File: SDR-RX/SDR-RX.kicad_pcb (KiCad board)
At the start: 2 copper layers, 53 x 51 mm, 49 parts, among them Q1 S8050, Q2 S8050, U1 Si4734-D60-GU, U2 ESP32-WROOM-32, U3 LD1117S33TR_SOT223, Y1 32.768kHz

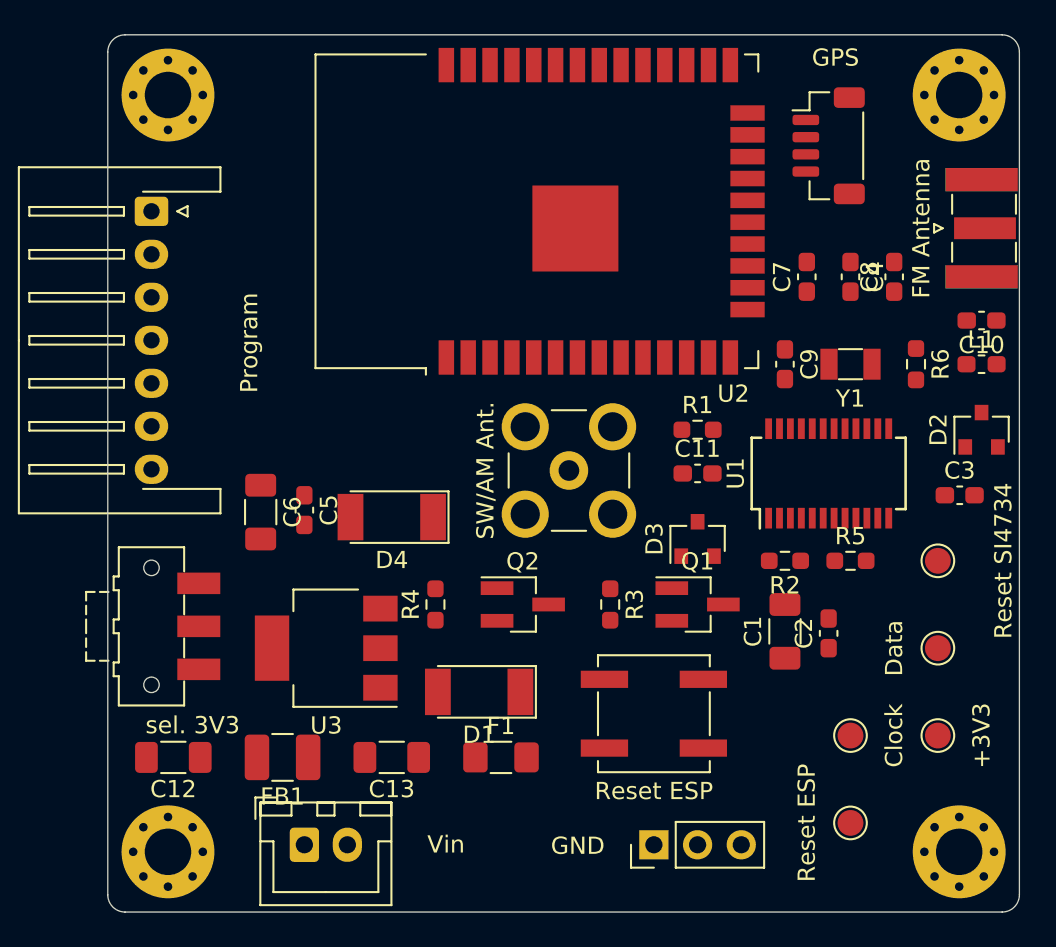
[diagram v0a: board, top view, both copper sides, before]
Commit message: routed without GND
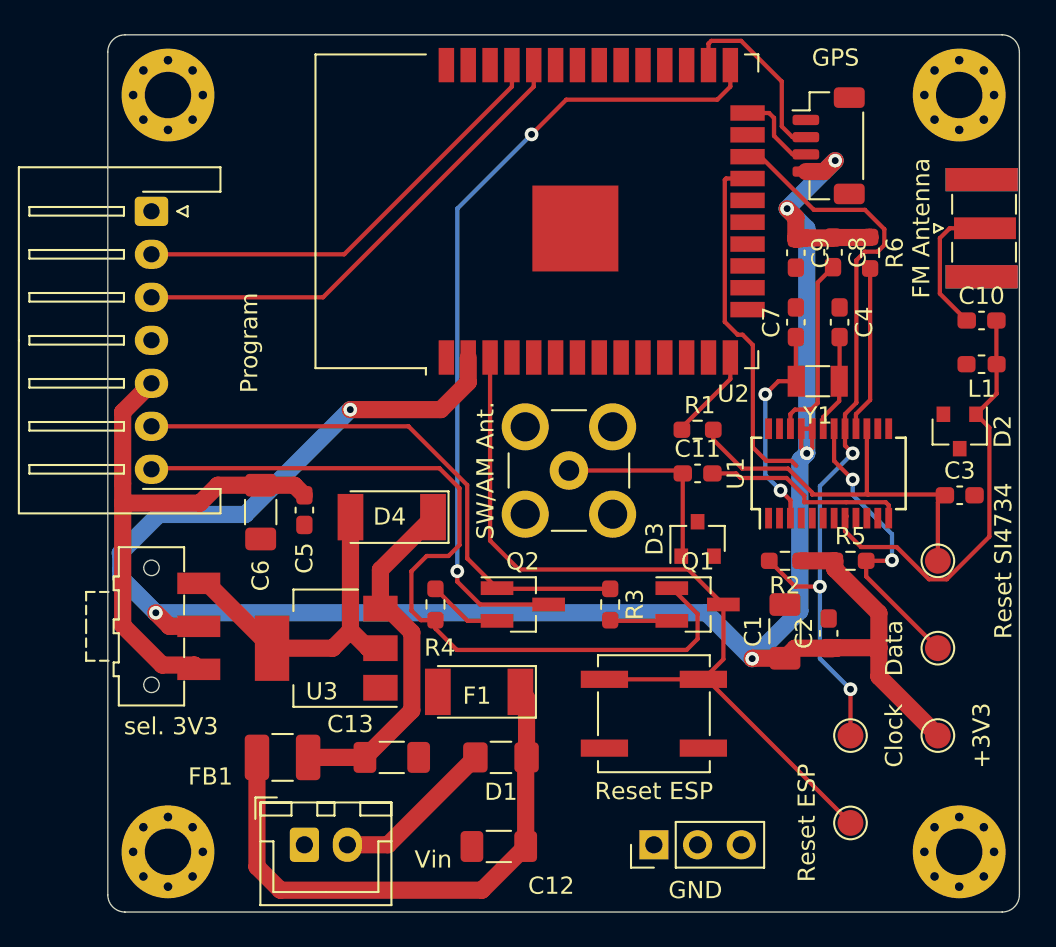
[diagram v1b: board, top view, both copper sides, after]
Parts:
- moved C12 19.6 mm to (398.4, 92.9)
- moved R6 7.00 mm to (420.0, 58.3)
- moved C9 6.51 mm to (415.7, 58.3)
- moved C8 3.83 mm to (417.9, 58.3), turned to 270 degrees
- moved C4 2.72 mm to (418.2, 62.4)
- moved C7 2.72 mm to (415.7, 62.4)
- moved Y1 2.15 mm to (417.0, 65.8)
- moved D2 1.27 mm to (425.2, 68.7), turned to 270 degrees
- turned C10 to 0 degrees
- turned C13 to 0 degrees
- turned L1 to 180 degrees
- turned R1 to 180 degrees
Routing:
- net +3V3: track 0.00 -> 135.1 mm, vias 0 -> 6
- net Net-(J1-Pad7): track 0.00 -> 49.1 mm
- net Net-(Q1-Pad3): track 0.00 -> 48.3 mm
- net Net-(Q2-Pad3): track 0.00 -> 47.6 mm, vias 0 -> 2
- net Net-(R2-Pad2): track 0.00 -> 45.9 mm, vias 0 -> 3
- net Net-(R5-Pad2): track 0.00 -> 38.8 mm, vias 0 -> 2
- net Net-(J1-Pad6): track 0.00 -> 33.1 mm
- net Net-(C12-Pad1): track 0.00 -> 32.8 mm
- net Net-(C5-Pad1): track 0.00 -> 32.0 mm
- net Net-(J1-Pad3): track 0.00 -> 28.5 mm
- net Net-(J1-Pad2): track 0.00 -> 26.2 mm
- net Net-(C10-Pad2): track 0.00 -> 24.9 mm
- net Net-(C3-Pad1): track 0.00 -> 23.3 mm
- net Net-(C13-Pad1): track 0.00 -> 20.7 mm
- net Net-(D4-Pad2): track 0.00 -> 19.6 mm
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
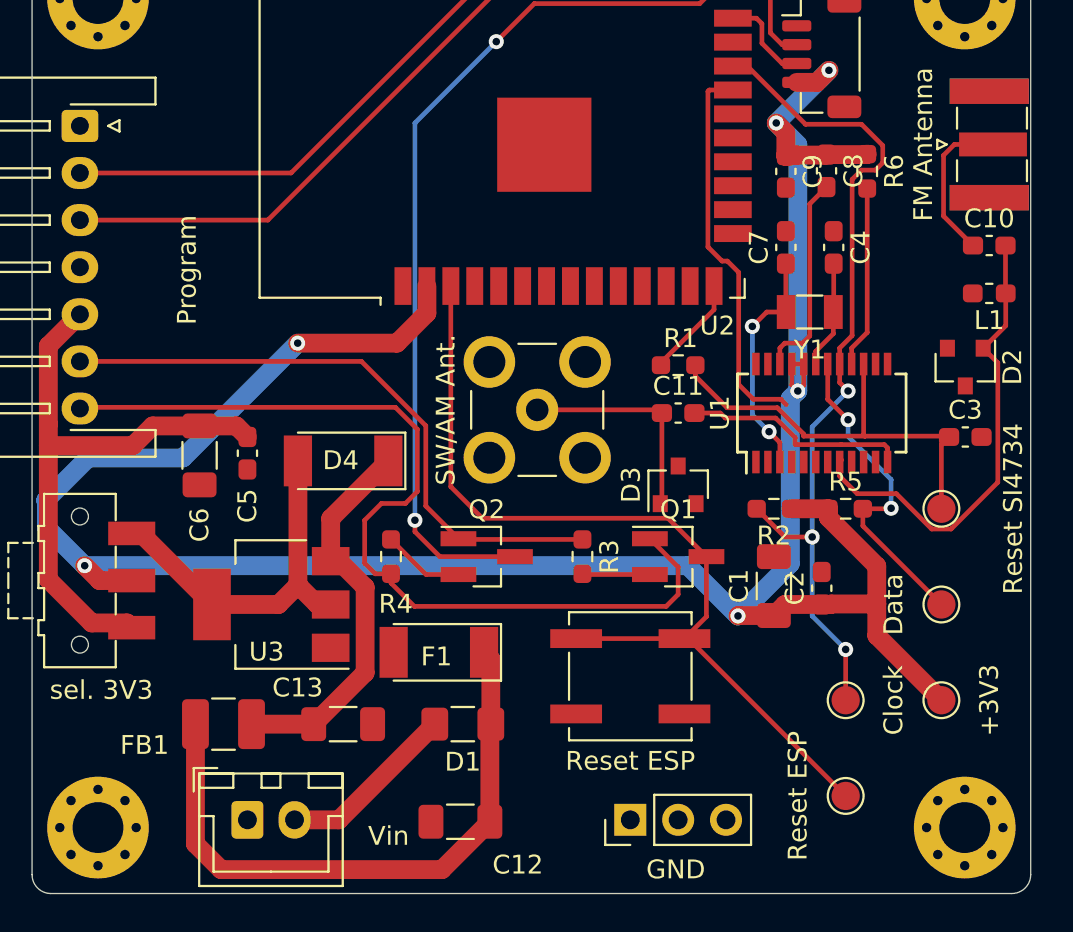
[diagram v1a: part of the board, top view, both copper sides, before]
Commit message: closed misssing copper
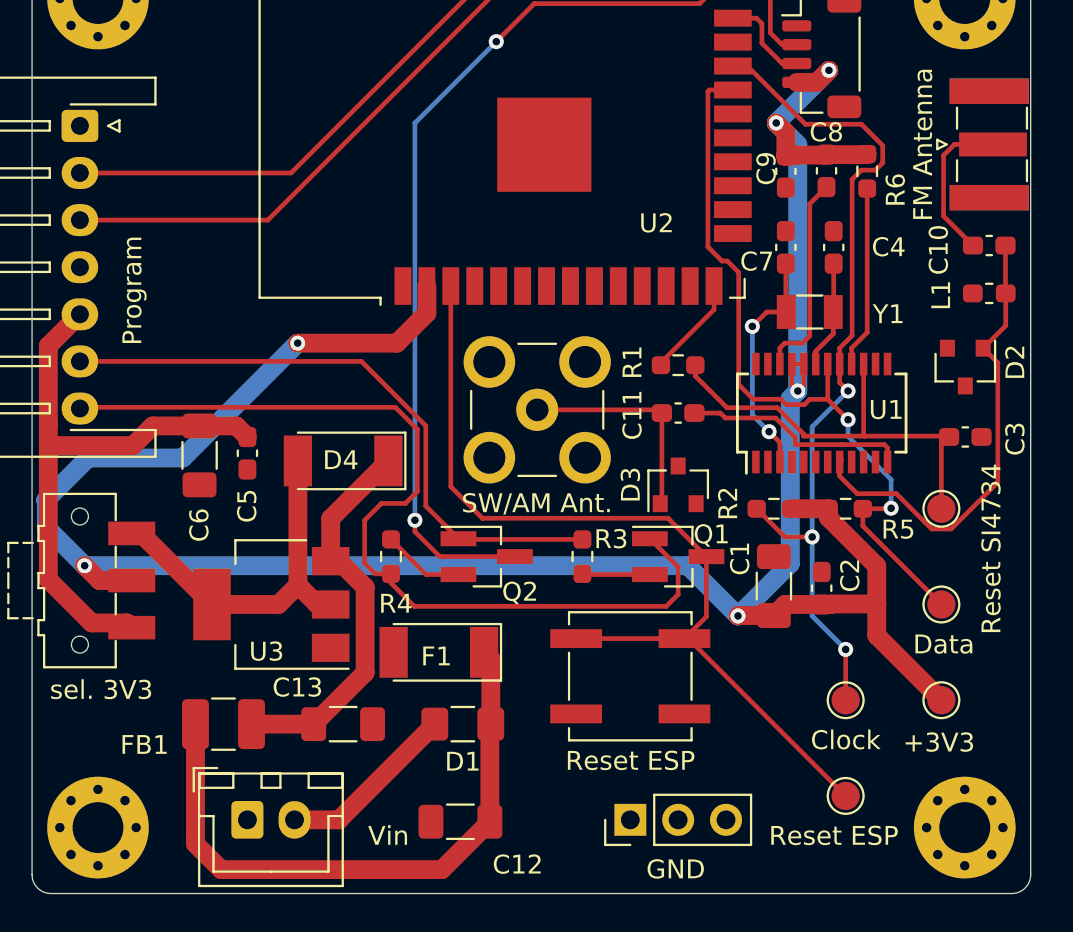
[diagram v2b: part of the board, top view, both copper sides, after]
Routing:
- net Net-(R5-Pad2): track 38.8 -> 41.1 mm

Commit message: PCB routed
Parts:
- added ?: , , F.Cu at (410.0, 95.4)
- moved Vin  1.27 mm to (388.4, 92.8)
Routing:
- net GND: track 0.00 -> 63.8 mm, vias 0 -> 20
- net +3V3: track 135.1 -> 118.8 mm
- net Net-(J1-Pad6): track 33.1 -> 35.0 mm
- net Net-(J1-Pad3): track 28.5 -> 30.1 mm, vias 0 -> 1
- net Net-(J1-Pad2): track 26.2 -> 27.6 mm, vias 0 -> 1
- net Net-(F1-Pad1): track 9.55 -> 8.28 mm
- net Net-(Q2-Pad3): track 47.6 -> 46.9 mm
- added copper zone on B.Cu, net GND
- added copper zone on F.Cu, net GND
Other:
- board text added: "3V3"
- board text added: "DTR"
- board text added: "GND"
- board text added: "NC"
- board text added: "RTS"
- board text added: "RX"
- board text added: "Rst SI4734"
- board text added: "TX"
- board text added: "Vin"

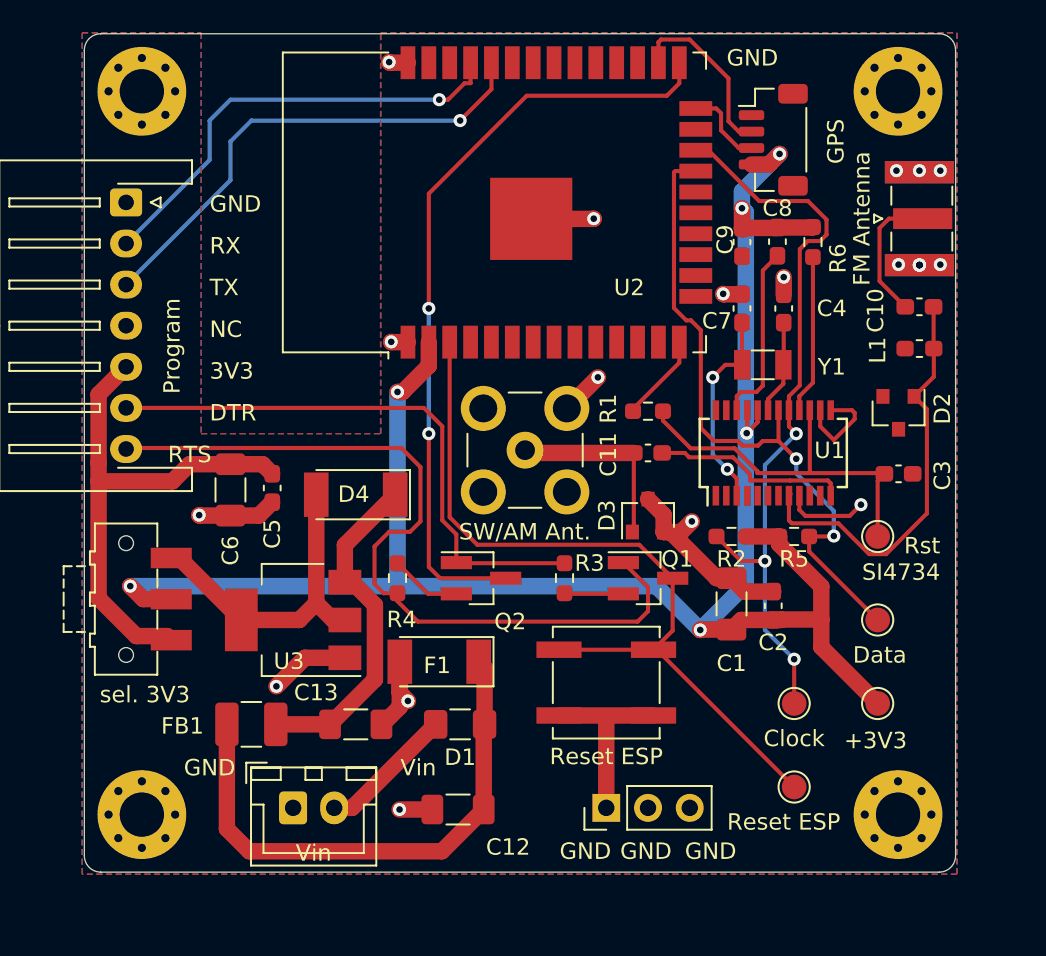
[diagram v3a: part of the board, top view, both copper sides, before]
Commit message: sticked back and front GND zones with vias
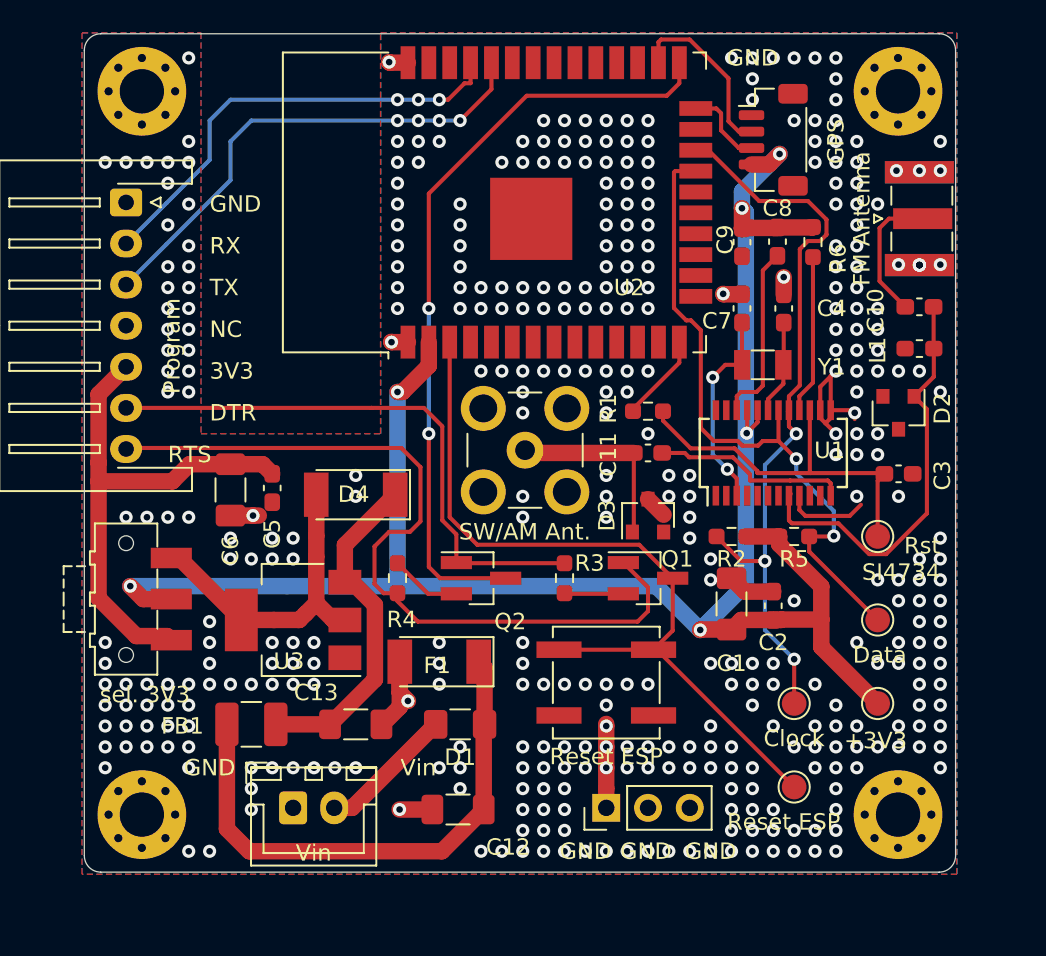
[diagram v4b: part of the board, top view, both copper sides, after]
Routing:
- net GND: track 63.8 -> 39.4 mm, vias 20 -> 395
- net Net-(J1-Pad2): vias 1 -> 3
- net Net-(J1-Pad3): vias 1 -> 4

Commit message: removed obsolete GND vias
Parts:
- moved C2 266.1 mm to (152.2, 99.5)
- moved C3 266.1 mm to (159.8, 91.5)
- moved D2 266.1 mm to (159.8, 87.8)
- moved GPS 266.1 mm to (152.2, 71.2)
- moved U1 266.1 mm to (152.2, 90.2)
- moved ? 266.1 mm to (144.6, 114.5)
- moved C1 266.1 mm to (149.6, 99.4)
- moved C10 266.1 mm to (161.1, 81.3)
- moved C11 266.1 mm to (144.6, 90.2)
- moved C12 266.1 mm to (133.0, 111.9)
- moved C13 266.1 mm to (126.8, 106.7)
- moved C4 266.1 mm to (152.8, 81.4)
- moved C5 266.1 mm to (121.7, 92.4)
- moved C7 266.1 mm to (150.3, 81.4)
- moved C9 266.1 mm to (150.3, 77.4)
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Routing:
- net GND: vias 395 -> 182
- net Net-(J1-Pad3): vias 4 -> 1
- net Net-(J1-Pad2): vias 3 -> 1

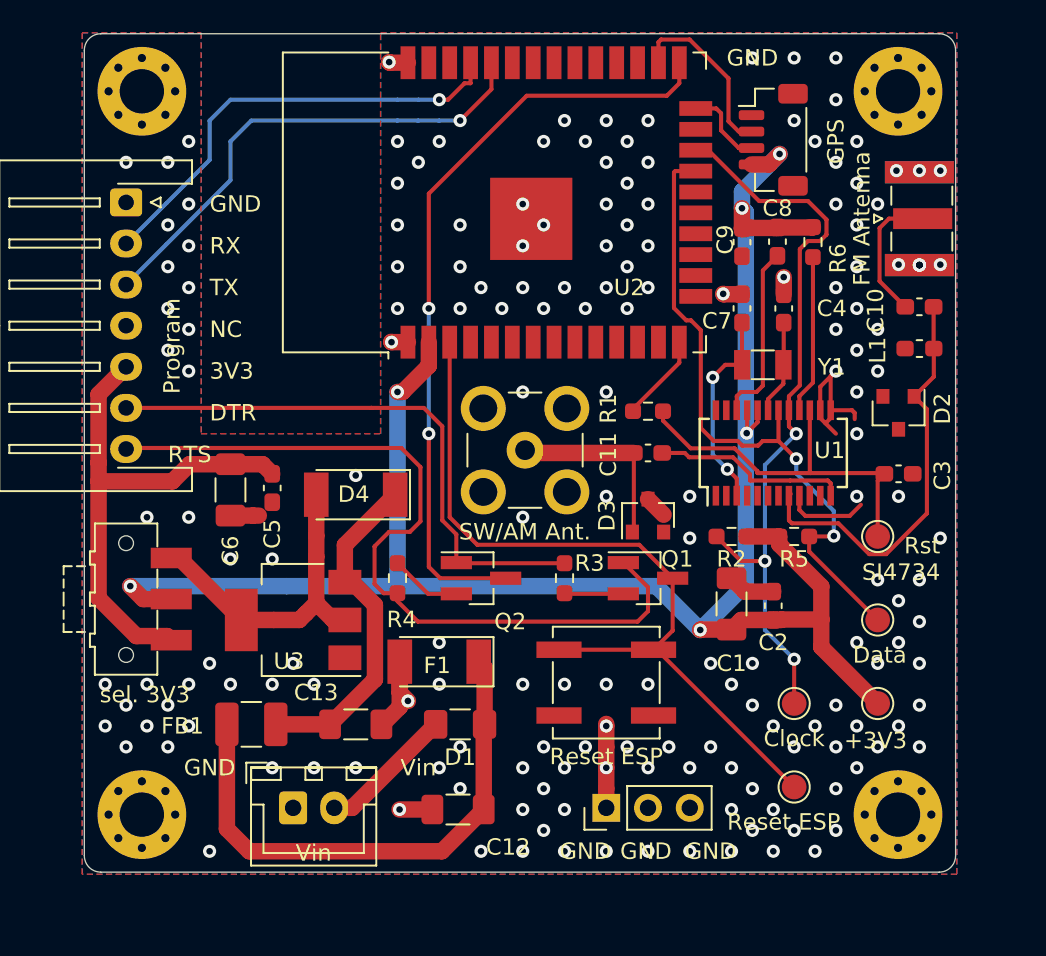
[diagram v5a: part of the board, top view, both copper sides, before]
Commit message: Added BOM and schematics.pdf
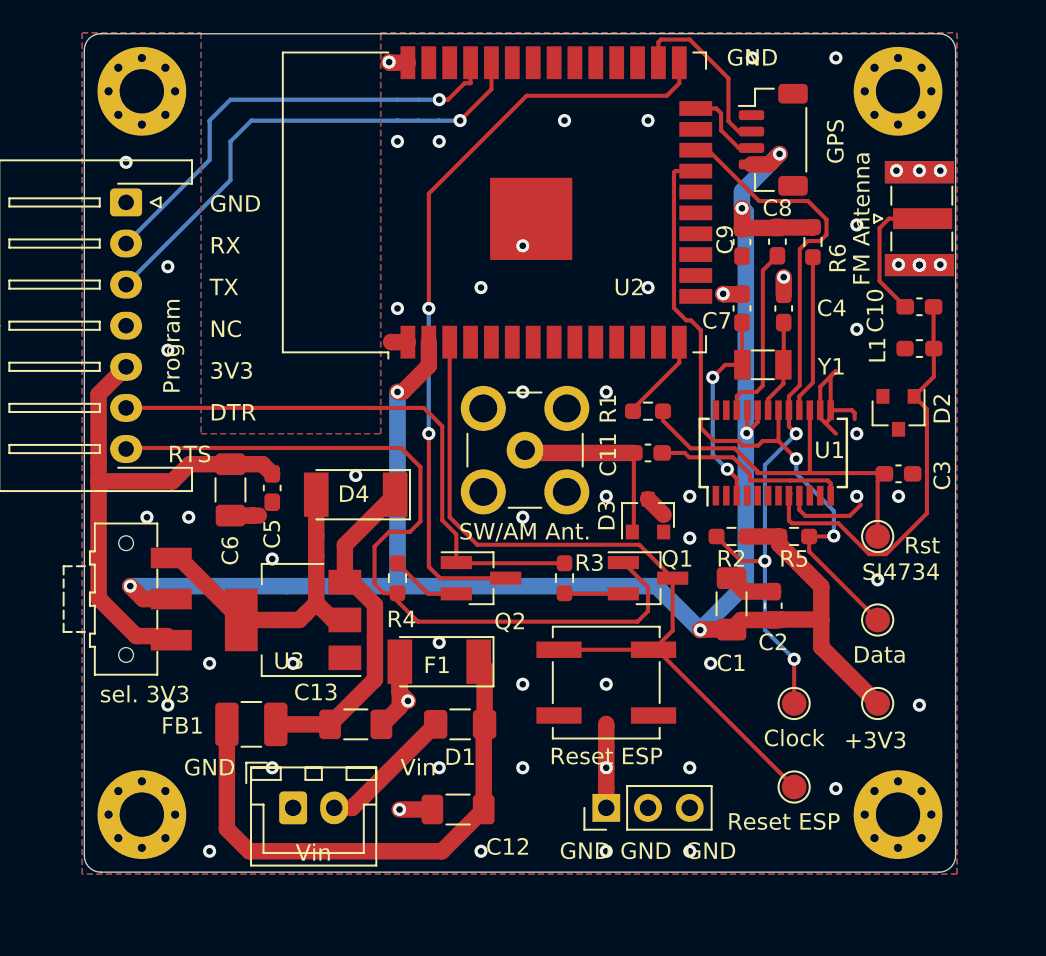
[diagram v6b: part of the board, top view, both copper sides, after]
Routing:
- net GND: vias 182 -> 60

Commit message: Added silk-screen text and logo
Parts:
- added G***: LOGO, hb9uf:hb9uf_logo_mid, B.Cu at (123.0, 77.1)
- added OSHW: Symbol_OSHW-Logo_SilkScreen_07Jul2012, hb9uf:Symbol_OSHW-Logo_SilkScreen, B.Cu at (123.0, 94.6)
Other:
- board text added: "HB9UF"
- board text added: "SDR-RX-PCB V1, radiation_pattern_drone (c) 2021 Daniel HB9GVD CC-BY-SA"

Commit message: some local files  deleted to regain last SDR-RX.kicad_pcb merged monday with frv branch
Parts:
- removed OSHW: Symbol_OSHW-Logo_SilkScreen_07Jul2012, hb9uf:Symbol_OSHW-Logo_SilkScreen
- moved G*** 0.31 mm to (122.7, 77.3)
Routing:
- net Net-(J1-Pad3): track 30.1 -> 36.6 mm
- net Net-(J1-Pad2): track 27.6 -> 32.6 mm
- net Net-(J1-Pad6): track 35.0 -> 36.1 mm
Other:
- board text added: "HB9UF HB9UHF"
- board text removed: "HB9UF"
- board text removed: "SDR-RX-PCB V1, radiation_pattern_drone (c) 2021 Daniel HB9GVD CC-BY-SA"
